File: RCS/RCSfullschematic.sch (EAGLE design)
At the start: 74 parts, among them IC1 ILD213T, IC2 FT232RL, J2 MOTOR, J4 POWER, J5 SENSORS, J7 USB-MICROB, Q2 8 MHz, T1 MMBT2222A, U1 MPL3115A2, U2 MPU-9250, U3 ATMEGA328P_TQFP, U4 ADS1015

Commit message: changed header
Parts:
- MCU: device SparkFun-Connectors:M04PTH -> SparkFun-Connectors:M03PTH
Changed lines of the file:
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@@
 <?xml version="1.0" encoding="utf-8"?>
 <!DOCTYPE eagle SYSTEM "eagle.dtd">
-<eagle version="7.7.0">
+<eagle version="7.5.0">
 <drawing>
 <settings>
@@
 <part name="MPWR" library="SparkFun-Connectors" deviceset="M02" device="PTH"/>
 <part name="R4" library="SparkFun-Passives" deviceset="RESISTOR" device="1206" value="1.2k"/>
-<part name="MCU" library="SparkFun-Connectors" deviceset="M04" device="PTH"/>
+<part name="MCU" library="SparkFun-Connectors" deviceset="M03" device="PTH"/>
 <part name="POT" library="SparkFun-Connectors" deviceset="M03" device="PTH"/>
 <part name="R5" library="adafruit" deviceset="R-US_" device="R1206" value="10k"/>
@@
 <instance part="MPWR" gate="G$1" x="271.78" y="30.48" rot="R180"/>
 <instance part="R4" gate="G$1" x="177.8" y="109.22" rot="R180"/>
-<instance part="MCU" gate="G$1" x="137.16" y="109.22"/>
+<instance part="MCU" gate="J$1" x="137.16" y="109.22"/>
 <instance part="POT" gate="J$1" x="210.82" y="111.76" rot="R180"/>
 <instance part="R5" gate="G$1" x="439.42" y="81.28" rot="R90"/>
@@
 </segment>
 <segment>
-<pinref part="MCU" gate="G$1" pin="3"/>
+<pinref part="MCU" gate="J$1" pin="3"/>
 <label x="144.78" y="111.76" size="1.778" layer="95"/>
-<wire x1="142.24" y1="111.76" x2="160.02" y2="111.76" width="0.1524" layer="91"/>
+<wire x1="144.78" y1="111.76" x2="160.02" y2="111.76" width="0.1524" layer="91"/>
 <wire x1="160.02" y1="111.76" x2="170.18" y2="111.76" width="0.1524" layer="91"/>
 <wire x1="170.18" y1="111.76" x2="170.18" y2="109.22" width="0.1524" layer="91"/>
@@
 </segment>
 <segment>
-<pinref part="MCU" gate="G$1" pin="2"/>
+<pinref part="MCU" gate="J$1" pin="2"/>
 <label x="144.78" y="109.22" size="1.778" layer="95"/>
-<wire x1="142.24" y1="109.22" x2="167.64" y2="109.22" width="0.1524" layer="91"/>
+<wire x1="144.78" y1="109.22" x2="167.64" y2="109.22" width="0.1524" layer="91"/>
 <wire x1="167.64" y1="109.22" x2="167.64" y2="104.14" width="0.1524" layer="91"/>
 <pinref part="R1" gate="G$1" pin="1"/>
@@
 </segment>
 <segment>
-<pinref part="MCU" gate="G$1" pin="1"/>
+<pinref part="MCU" gate="J$1" pin="1"/>
 <label x="144.78" y="106.68" size="1.778" layer="95"/>
-<wire x1="142.24" y1="106.68" x2="190.5" y2="106.68" width="0.1524" layer="91"/>
+<wire x1="144.78" y1="106.68" x2="190.5" y2="106.68" width="0.1524" layer="91"/>
 <wire x1="190.5" y1="106.68" x2="190.5" y2="111.76" width="0.1524" layer="91"/>
 <pinref part="POT" gate="J$1" pin="2"/>

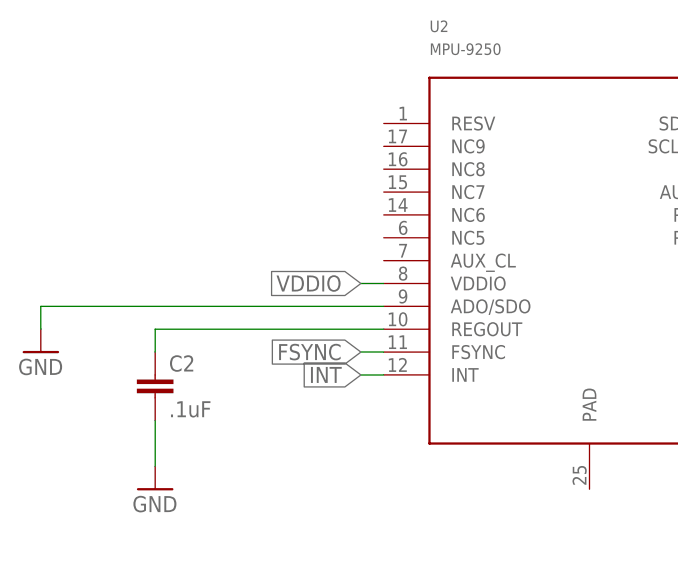
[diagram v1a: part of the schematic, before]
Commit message: Changed VDD to LOGIC_VDD
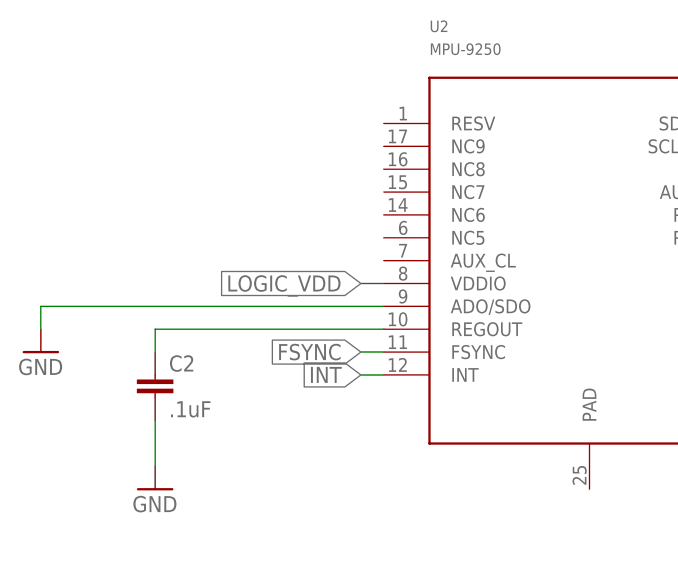
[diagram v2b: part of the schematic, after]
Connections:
- net LOGIC_VDD: now also U2.VDDIO
- net VDDIO: no longer U2.VDDIO
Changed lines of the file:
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@@
 <?xml version="1.0" encoding="utf-8"?>
 <!DOCTYPE eagle SYSTEM "eagle.dtd">
-<eagle version="7.5.0">
+<eagle version="7.6.0">
 <drawing>
 <settings>
@@
 <label x="38.1" y="116.84" size="1.778" layer="95" rot="R180" xref="yes"/>
 </segment>
-<segment>
-<pinref part="U2" gate="G$1" pin="VDDIO"/>
-<wire x1="-99.06" y1="15.24" x2="-101.6" y2="15.24" width="0.1524" layer="91"/>
-<label x="-101.6" y="15.24" size="1.778" layer="95" rot="R180" xref="yes"/>
-</segment>
 </net>
 <net name="ADO/SDO" class="0">
@@
 <label x="198.12" y="114.3" size="1.778" layer="95" rot="R180" xref="yes"/>
 </segment>
-</net>
+<segment>
+<pinref part="U2" gate="G$1" pin="VDDIO"/>
+<wire x1="-99.06" y1="15.24" x2="-101.6" y2="15.24" width="0.1524" layer="91"/>
+<label x="-101.6" y="15.24" size="1.778" layer="95" rot="R180" xref="yes"/>
+</segment>
+</net>

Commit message: yep
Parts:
- F1: value 3A -> TRIP 1.5A; device SparkFun-PowerIC:PTCSMD -> fuse:PICOFUSE
- F3: value TRIP 0.1A -> TRIP 100mA
- F4: value TRIP 1.7A -> TRIP 1.5A
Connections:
- net GND_MOTOR renamed GND1
- net N$4: now also F1.1; no longer F1.2
- net VOUT-MOTOR: now also F1.2; no longer F1.1

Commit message: change
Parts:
- removed JP2: MCU, SparkFun-Connectors:M02PTH
- removed JP3: 11.1V, SparkFun-Connectors:M02JST-PTH-2
- removed JP4: 7.4V, SparkFun-Connectors:M02JST-PTH-2
- added MPWR1: 11.1, SparkFun-Connectors:M02PTH
- added MPWR2: 7.4V, SparkFun-Connectors:M02PTH
- JP1: value SENSOR -> SENSOR/MCU
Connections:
- net GND: now also MPWR2.1; no longer JP2.2, JP3.1
- net GND1: now also MPWR1.1; no longer JP4.1
- net LOGIC_VDD: no longer JP2.1
- net N$16: now also MPWR2.2; no longer JP3.2
- net N$19: now also MPWR1.2; no longer JP4.2
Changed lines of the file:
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@@
 <part name="F3" library="fuse" deviceset="PICOFUSE" device="" value="TRIP 100mA"/>
 <part name="GND" library="SparkFun-Aesthetics" deviceset="GND" device="" value=""/>
-<part name="JP1" library="SparkFun-Connectors" deviceset="M02" device="PTH" value="SENSOR"/>
-<part name="JP2" library="SparkFun-Connectors" deviceset="M02" device="PTH" value="MCU"/>
-<part name="JP3" library="SparkFun-Connectors" deviceset="M02" device="JST-PTH-2" value="11.1V"/>
+<part name="JP1" library="SparkFun-Connectors" deviceset="M02" device="PTH" value="SENSOR/MCU"/>
 <part name="SW2" library="special" deviceset="SW_DIP-1" device=""/>
 <part name="R12" library="rcl" deviceset="R-US_" device="M1206" value="180"/>
@@
 <part name="C14" library="SparkFun-Capacitors" deviceset="10UF-POLAR" device="-EIA3216-16V-10%(TANT)" value="10uF"/>
 <part name="LM117" library="v-reg" deviceset="LM317-T039" device=""/>
-<part name="JP4" library="SparkFun-Connectors" deviceset="M02" device="JST-PTH-2" value="7.4V"/>
 <part name="SW3" library="special" deviceset="SW_DIP-1" device=""/>
 <part name="F4" library="fuse" deviceset="PICOFUSE" device="" value="TRIP 1.5A"/>
@@
 <part name="F1" library="fuse" deviceset="PICOFUSE" device="" value="TRIP 1.5A"/>
 <part name="SUPPLY1" library="supply2" deviceset="GND1" device=""/>
+<part name="MPWR1" library="SparkFun-Connectors" deviceset="M02" device="PTH" value="11.1"/>
+<part name="MPWR2" library="SparkFun-Connectors" deviceset="M02" device="PTH" value="7.4V"/>
 </parts>
 <sheets>
@@
 <instance part="GND" gate="1" x="271.78" y="177.8"/>
 <instance part="JP1" gate="G$1" x="383.54" y="215.9" rot="R180"/>
-<instance part="JP2" gate="G$1" x="383.54" y="198.12" rot="R180"/>
-<instance part="JP3" gate="G$1" x="203.2" y="208.28"/>
 <instance part="SW2" gate="G$1" x="236.22" y="220.98"/>
 <instance part="R12" gate="G$1" x="312.42" y="198.12" rot="R90"/>
@@
 <instance part="C14" gate="G$1" x="340.36" y="205.74"/>
 <instance part="LM117" gate="G$1" x="312.42" y="220.98"/>
-<instance part="JP4" gate="G$1" x="203.2" y="243.84"/>
 <instance part="SW3" gate="G$1" x="231.14" y="256.54"/>
 <instance part="F4" gate="1" x="261.62" y="256.54"/>
@@
 <instance part="F1" gate="1" x="226.06" y="30.48"/>
 <instance part="SUPPLY1" gate="G$1" x="271.78" y="223.52"/>
+<instance part="MPWR1" gate="G$1" x="203.2" y="243.84"/>
+<instance part="MPWR2" gate="G$1" x="203.2" y="208.28"/>
 </instances>
 <busses>
@@
 </segment>
 <segment>
-<pinref part="JP2" gate="G$1" pin="2"/>
-<wire x1="375.92" y1="195.58" x2="370.84" y2="195.58" width="0.1524" layer="91"/>
-<label x="370.84" y="195.58" size="1.016" layer="95" rot="R180" xref="yes"/>
-</segment>
-<segment>
 <wire x1="312.42" y1="190.5" x2="340.36" y2="190.5" width="0.1524" layer="91"/>
 <wire x1="340.36" y1="190.5" x2="347.98" y2="190.5" width="0.1524" layer="91"/>
@@
 <label x="261.62" y="177.8" size="1.778" layer="95"/>
 <label x="350.52" y="190.5" size="1.778" layer="95" xref="yes"/>
-<pinref part="JP3" gate="G$1" pin="1"/>
 <wire x1="210.82" y1="208.28" x2="210.82" y2="190.5" width="0.1524" layer="91"/>
 <pinref part="D1" gate="G$1" pin="A"/>
@@
 <pinref part="C13" gate="G$1" pin="-"/>
 <pinref part="C14" gate="G$1" pin="-"/>
+<pinref part="MPWR2" gate="G$1" pin="1"/>
 </segment>
 </net>
@@
 </segment>
 <segment>
-<pinref part="JP2" gate="G$1" pin="1"/>
-<wire x1="375.92" y1="198.12" x2="370.84" y2="198.12" width="0.1524" layer="91"/>
-<label x="370.84" y="198.12" size="1.016" layer="95" rot="R180" xref="yes"/>
-</segment>
-<segment>
 <pinref part="POT" gate="J$1" pin="1"/>
 <wire x1="203.2" y1="114.3" x2="198.12" y2="114.3" width="0.1524" layer="91"/>
@@
 <net name="N$16" class="0">
 <segment>
-<pinref part="JP3" gate="G$1" pin="2"/>
-<wire x1="210.82" y1="210.82" x2="210.82" y2="220.98" width="0.1524" layer="91"/>
 <pinref part="SW2" gate="G$1" pin="2"/>
 <wire x1="210.82" y1="220.98" x2="228.6" y2="220.98" width="0.1524" layer="91"/>
+<pinref part="MPWR2" gate="G$1" pin="2"/>
+<wire x1="210.82" y1="220.98" x2="210.82" y2="210.82" width="0.1524" layer="91"/>
 </segment>
 </net>
@@
 <net name="N$19" class="0">
 <segment>
-<pinref part="JP4" gate="G$1" pin="2"/>
 <wire x1="210.82" y1="246.38" x2="210.82" y2="256.54" width="0.1524" layer="91"/>
 <pinref part="SW3" gate="G$1" pin="2"/>
 <wire x1="210.82" y1="256.54" x2="223.52" y2="256.54" width="0.1524" layer="91"/>
+<pinref part="MPWR1" gate="G$1" pin="2"/>
 </segment>
 </net>
@@
 <wire x1="281.94" y1="228.6" x2="271.78" y2="228.6" width="0.1524" layer="91"/>
 <junction x="281.94" y="228.6"/>
-<pinref part="JP4" gate="G$1" pin="1"/>
 <wire x1="271.78" y1="228.6" x2="210.82" y2="228.6" width="0.1524" layer="91"/>
 <wire x1="210.82" y1="228.6" x2="210.82" y2="243.84" width="0.1524" layer="91"/>
@@
 <label x="355.6" y="228.6" size="1.27" layer="95" xref="yes"/>
 <pinref part="SUPPLY1" gate="G$1" pin="GND1"/>
-</segment>
-<segment>
+<pinref part="MPWR1" gate="G$1" pin="1"/>
+</segment>
+<segment>

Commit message: yep
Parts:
- removed D2: 6.1V, SparkFun-DiscreteSemi:DIODE-ZENER-BZT52C3V6S
- D1: value 3.45V -> 3.3V
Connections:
- net GND1: no longer D2.A
- net VOUT-MOTOR: no longer D2.C
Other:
- moved on the sheet: IC3
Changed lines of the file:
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@@
 <part name="R11" library="adafruit" deviceset="R-US_" device="R1206" value="10k"/>
 <part name="GND21" library="supply1" deviceset="GND" device=""/>
-<part name="D1" library="SparkFun-DiscreteSemi" deviceset="DIODE-ZENER" device="-BZT52C3V6S" value="3.45V"/>
+<part name="D1" library="SparkFun-DiscreteSemi" deviceset="DIODE-ZENER" device="-BZT52C3V6S" value="3.3V"/>
 <part name="F3" library="fuse" deviceset="PICOFUSE" device="" value="TRIP 100mA"/>
 <part name="GND" library="SparkFun-Aesthetics" deviceset="GND" device="" value=""/>
@@
 <part name="C16" library="SparkFun-Capacitors" deviceset="10UF-POLAR" device="-EIA3216-16V-10%(TANT)" value="10uF"/>
 <part name="C17" library="SparkFun-Capacitors" deviceset="10UF-POLAR" device="-EIA3216-16V-10%(TANT)" value="10uF"/>
-<part name="D2" library="SparkFun-DiscreteSemi" deviceset="DIODE-ZENER" device="-BZT52C3V6S" value="6.1V"/>
 <part name="IC3" library="v-reg" deviceset="LM317-T039" device=""/>
 <part name="R14" library="rcl" deviceset="R-US_" device="M1206" value="200"/>
@@
 <instance part="C16" gate="G$1" x="292.1" y="246.38"/>
 <instance part="C17" gate="G$1" x="337.82" y="246.38"/>
-<instance part="D2" gate="G$1" x="347.98" y="246.38" rot="R90"/>
-<instance part="IC3" gate="G$1" x="309.88" y="256.54"/>
+<instance part="IC3" gate="G$1" x="312.42" y="256.54"/>
 <instance part="R14" gate="G$1" x="327.66" y="246.38" rot="R90"/>
 <instance part="R15" gate="G$1" x="312.42" y="233.68" rot="R90"/>
@@
 <wire x1="292.1" y1="256.54" x2="292.1" y2="248.92" width="0.1524" layer="91"/>
 <pinref part="IC3" gate="G$1" pin="IN"/>
-<wire x1="292.1" y1="256.54" x2="302.26" y2="256.54" width="0.1524" layer="91"/>
+<wire x1="292.1" y1="256.54" x2="304.8" y2="256.54" width="0.1524" layer="91"/>
 <junction x="292.1" y="256.54"/>
 </segment>
@@
 <segment>
 <pinref part="IC3" gate="G$1" pin="ADJ"/>
-<wire x1="309.88" y1="248.92" x2="312.42" y2="241.3" width="0.1524" layer="91"/>
+<wire x1="312.42" y1="248.92" x2="312.42" y2="241.3" width="0.1524" layer="91"/>
 <pinref part="R15" gate="G$1" pin="2"/>
 <pinref part="R14" gate="G$1" pin="1"/>
@@
 <segment>
 <pinref part="IC3" gate="G$1" pin="OUT"/>
-<wire x1="317.5" y1="256.54" x2="327.66" y2="256.54" width="0.1524" layer="91"/>
+<wire x1="320.04" y1="256.54" x2="327.66" y2="256.54" width="0.1524" layer="91"/>
 <pinref part="C17" gate="G$1" pin="+"/>
 <wire x1="327.66" y1="256.54" x2="337.82" y2="256.54" width="0.1524" layer="91"/>
@@
 <wire x1="327.66" y1="251.46" x2="327.66" y2="256.54" width="0.1524" layer="91"/>
 <junction x="327.66" y="256.54"/>
-<wire x1="337.82" y1="256.54" x2="347.98" y2="256.54" width="0.1524" layer="91"/>
+<wire x1="337.82" y1="256.54" x2="355.6" y2="256.54" width="0.1524" layer="91"/>
 <junction x="337.82" y="256.54"/>
-<pinref part="D2" gate="G$1" pin="C"/>
-<wire x1="347.98" y1="256.54" x2="347.98" y2="248.92" width="0.1524" layer="91"/>
-<wire x1="347.98" y1="256.54" x2="355.6" y2="256.54" width="0.1524" layer="91"/>
-<junction x="347.98" y="256.54"/>
 <label x="355.6" y="256.54" size="1.27" layer="95" xref="yes"/>
 </segment>
@@
 <wire x1="337.82" y1="228.6" x2="312.42" y2="228.6" width="0.1524" layer="91"/>
 <junction x="312.42" y="228.6"/>
-<pinref part="D2" gate="G$1" pin="A"/>
-<wire x1="347.98" y1="243.84" x2="347.98" y2="228.6" width="0.1524" layer="91"/>
-<wire x1="347.98" y1="228.6" x2="337.82" y2="228.6" width="0.1524" layer="91"/>
+<wire x1="355.6" y1="228.6" x2="337.82" y2="228.6" width="0.1524" layer="91"/>
 <junction x="337.82" y="228.6"/>
-<wire x1="347.98" y1="228.6" x2="355.6" y2="228.6" width="0.1524" layer="91"/>
-<junction x="347.98" y="228.6"/>
 <label x="355.6" y="228.6" size="1.27" layer="95" xref="yes"/>
 <pinref part="SUPPLY1" gate="G$1" pin="GND1"/>

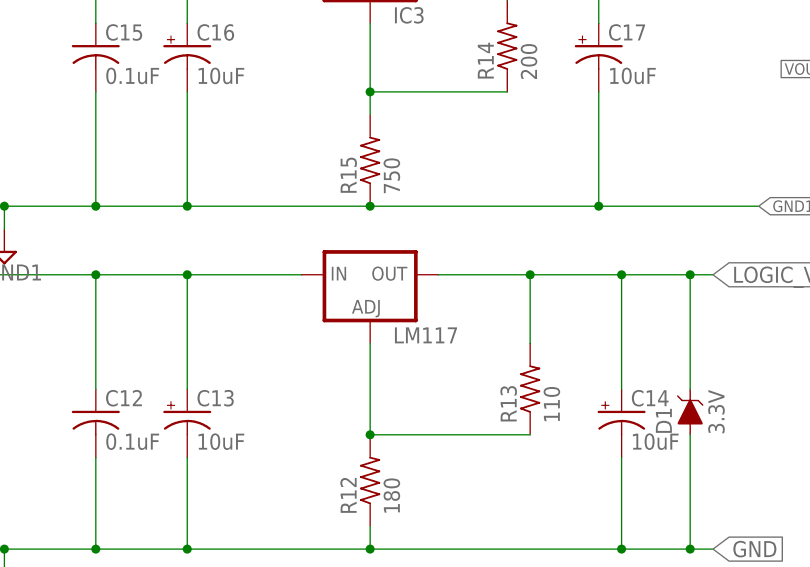
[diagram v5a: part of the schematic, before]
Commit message: one ic switched
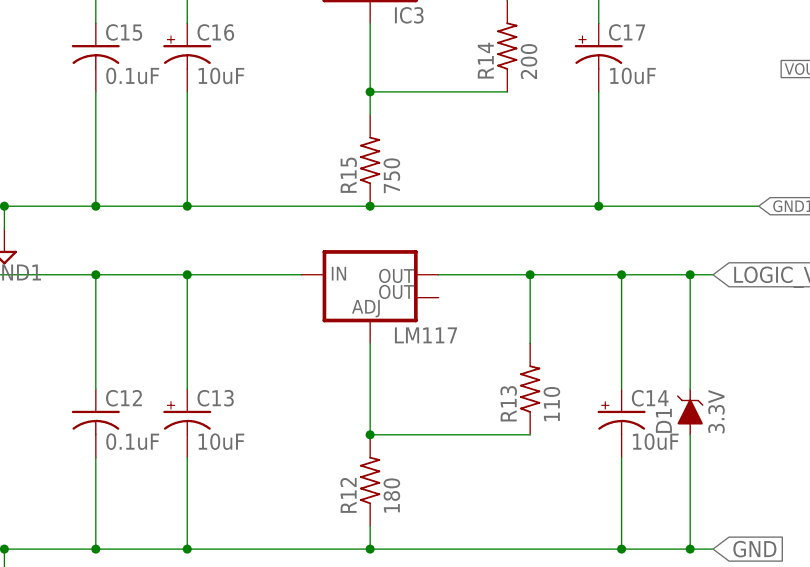
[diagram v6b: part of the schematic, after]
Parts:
- LM117: device v-reg:LM317-T039 -> SparkFun-IC-Power:V_REG_LM1117SOT223
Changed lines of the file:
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@@
 <part name="C13" library="SparkFun-Capacitors" deviceset="10UF-POLAR" device="-EIA3216-16V-10%(TANT)" value="10uF"/>
 <part name="C14" library="SparkFun-Capacitors" deviceset="10UF-POLAR" device="-EIA3216-16V-10%(TANT)" value="10uF"/>
-<part name="LM117" library="v-reg" deviceset="LM317-T039" device=""/>
+<part name="LM117" library="SparkFun-IC-Power" deviceset="V_REG_LM1117" device="SOT223"/>
 <part name="SW3" library="special" deviceset="SW_DIP-1" device=""/>
 <part name="F4" library="fuse" deviceset="PICOFUSE" device="" value="TRIP 1.5A"/>

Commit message: k
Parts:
- removed IC3: (no value), v-reg:LM317-T039
- added IC4: 317T, linear:317T
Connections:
- net N$21: now also IC4.VI; no longer IC3.IN
- net N$22: now also IC4.ADJ; no longer IC3.ADJ
- net VOUT-MOTOR: now also IC4.VO; no longer IC3.OUT
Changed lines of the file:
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@@
 <part name="C16" library="SparkFun-Capacitors" deviceset="10UF-POLAR" device="-EIA3216-16V-10%(TANT)" value="10uF"/>
 <part name="C17" library="SparkFun-Capacitors" deviceset="10UF-POLAR" device="-EIA3216-16V-10%(TANT)" value="10uF"/>
-<part name="IC3" library="v-reg" deviceset="LM317-T039" device=""/>
 <part name="R14" library="rcl" deviceset="R-US_" device="M1206" value="200"/>
 <part name="R15" library="rcl" deviceset="R-US_" device="M1206" value="750"/>
@@
 <part name="MPWR1" library="SparkFun-Connectors" deviceset="M02" device="PTH" value="11.1"/>
 <part name="MPWR2" library="SparkFun-Connectors" deviceset="M02" device="PTH" value="7.4V"/>
+<part name="IC4" library="linear" deviceset="*317" device="T"/>
 </parts>
 <sheets>
@@
 <instance part="C16" gate="G$1" x="292.1" y="246.38"/>
 <instance part="C17" gate="G$1" x="337.82" y="246.38"/>
-<instance part="IC3" gate="G$1" x="312.42" y="256.54"/>
 <instance part="R14" gate="G$1" x="327.66" y="246.38" rot="R90"/>
 <instance part="R15" gate="G$1" x="312.42" y="233.68" rot="R90"/>
@@
 <instance part="MPWR1" gate="G$1" x="203.2" y="243.84"/>
 <instance part="MPWR2" gate="G$1" x="203.2" y="208.28"/>
+<instance part="IC4" gate="A1" x="312.42" y="254"/>
 </instances>
 <busses>
@@
 <pinref part="C16" gate="G$1" pin="+"/>
 <wire x1="292.1" y1="256.54" x2="292.1" y2="248.92" width="0.1524" layer="91"/>
-<pinref part="IC3" gate="G$1" pin="IN"/>
-<wire x1="292.1" y1="256.54" x2="304.8" y2="256.54" width="0.1524" layer="91"/>
+<pinref part="IC4" gate="A1" pin="VI"/>
+<wire x1="292.1" y1="256.54" x2="302.26" y2="256.54" width="0.1524" layer="91"/>
 <junction x="292.1" y="256.54"/>
 </segment>
@@
 <net name="N$22" class="0">
 <segment>
-<pinref part="IC3" gate="G$1" pin="ADJ"/>
-<wire x1="312.42" y1="248.92" x2="312.42" y2="241.3" width="0.1524" layer="91"/>
 <pinref part="R15" gate="G$1" pin="2"/>
 <pinref part="R14" gate="G$1" pin="1"/>
 <wire x1="312.42" y1="241.3" x2="312.42" y2="238.76" width="0.1524" layer="91"/>
 <wire x1="327.66" y1="241.3" x2="312.42" y2="241.3" width="0.1524" layer="91"/>
+<pinref part="IC4" gate="A1" pin="ADJ"/>
+<wire x1="312.42" y1="248.92" x2="312.42" y2="241.3" width="0.1524" layer="91"/>
 <junction x="312.42" y="241.3"/>
 </segment>
@@
 <net name="VOUT-MOTOR" class="0">
 <segment>
-<pinref part="IC3" gate="G$1" pin="OUT"/>
-<wire x1="320.04" y1="256.54" x2="327.66" y2="256.54" width="0.1524" layer="91"/>
 <pinref part="C17" gate="G$1" pin="+"/>
 <wire x1="327.66" y1="256.54" x2="337.82" y2="256.54" width="0.1524" layer="91"/>
@@
 <pinref part="R14" gate="G$1" pin="2"/>
 <wire x1="327.66" y1="251.46" x2="327.66" y2="256.54" width="0.1524" layer="91"/>
-<junction x="327.66" y="256.54"/>
 <wire x1="337.82" y1="256.54" x2="355.6" y2="256.54" width="0.1524" layer="91"/>
 <junction x="337.82" y="256.54"/>
 <label x="355.6" y="256.54" size="1.27" layer="95" xref="yes"/>
-</segment>
-<segment>
+<pinref part="IC4" gate="A1" pin="VO"/>
+<wire x1="322.58" y1="256.54" x2="327.66" y2="256.54" width="0.1524" layer="91"/>
+<junction x="327.66" y="256.54"/>
+</segment>
+<segment>
